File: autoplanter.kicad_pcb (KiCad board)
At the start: 2 copper layers, 99.1 x 49.5 mm, 77 parts, among them IC1 KST10MTF, IC2 KST10MTF, IC3 BME680, IC4 MCP73842T-840I_UN, J1 water, J2 USB_C_Receptacle_USB2.0, J3 Conn_01x10_Female, J4 Conn_01x02_Female, K1 Y14x-1C-xxDS, M1 Motor_DC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

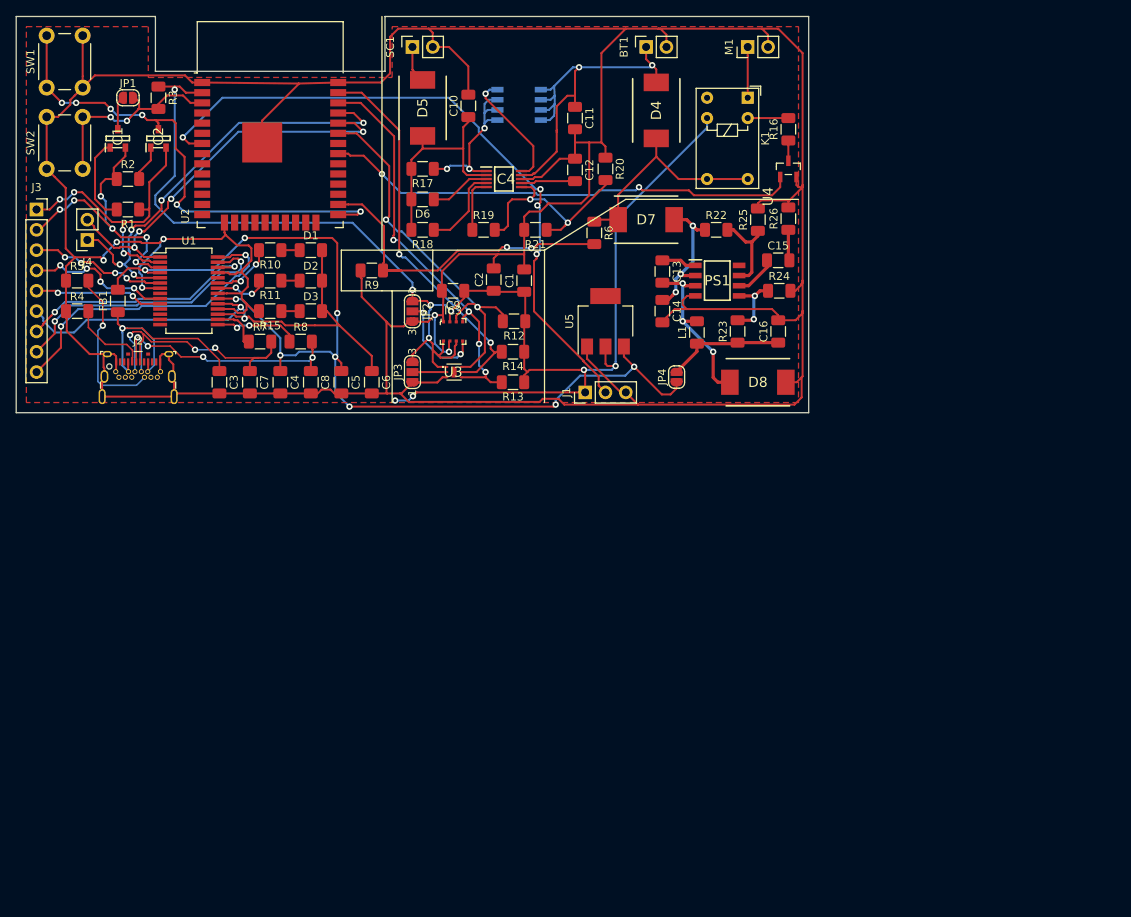
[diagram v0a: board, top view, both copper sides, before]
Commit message: Fixed regurator and added low voltage safe circuit.
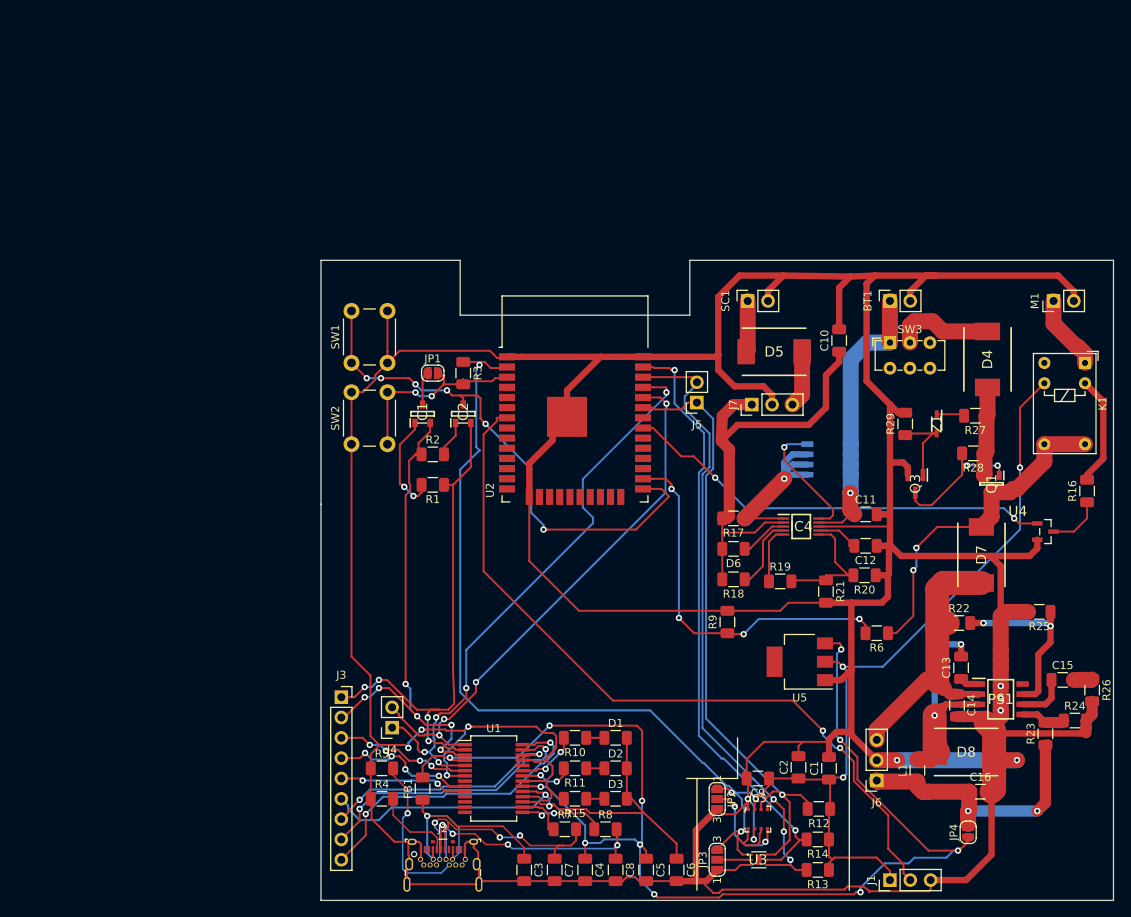
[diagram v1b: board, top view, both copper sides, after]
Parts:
- added J5: I2C Debug, Connector_PinSocket_2.54mm:PinSocket_1x02_P2.54mm_Vertical, F.Cu at (148.6, 73.7)
- added J6: external regurator, Connector_PinSocket_2.54mm:PinSocket_1x03_P2.54mm_Vertical, F.Cu at (171.1, 120.9)
- added J7: 12v regurator, Connector_PinHeader_2.54mm:PinHeader_1x03_P2.54mm_Vertical, F.Cu at (155.4, 73.9)
- added Q1: DMG2301L-7, SOT96P240X110-3N, F.Cu at (185.4, 83.8)
- added Q3: 2SC2712-Y,LF, SOT95P260X140-3N, F.Cu at (175.9, 83.8)
- added R27: 20k, Capacitor_SMD:C_1206_3216Metric, F.Cu at (183.4, 75.3)
- added R28: 20k, Capacitor_SMD:C_1206_3216Metric, F.Cu at (183.1, 80.0)
- added R29: 10k, Capacitor_SMD:C_1206_3216Metric, F.Cu at (174.6, 76.3)
- added SW3: SW_DIP_x01, Button_Switch_THT:SW_E-Switch_EG1271_DPDT, F.Cu at (172.7, 66.2)
- added Z1: MM3Z6V2T1G, SOD2512X110N, F.Cu at (178.6, 76.3)
- moved C4 71.9 mm to (134.6, 132.1)
- moved C5 71.9 mm to (142.2, 132.1)
- moved C6 71.9 mm to (146.1, 132.1)
- moved C7 71.9 mm to (130.8, 132.1)
- moved C8 71.9 mm to (138.4, 132.1)
- moved C9 71.9 mm to (156.2, 120.7)
- moved IC3 71.9 mm to (156.2, 125.7)
- moved U3 71.9 mm to (156.2, 130.8)
- moved C3 71.9 mm to (127.0, 132.1)
- moved D3 71.9 mm to (138.4, 123.2)
- moved JP3 71.9 mm to (151.1, 130.8)
- moved R13 71.9 mm to (163.7, 132.1)
- moved R14 71.9 mm to (163.7, 128.3)
- moved U1 71.9 mm to (123.2, 120.7)
- moved C2 71.9 mm to (161.3, 119.2)
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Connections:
- D4 pad 1: Net-(BT1-Pad1) -> Net-(D4-Pad1)
- D4 pad 2: +BATT -> Net-(D4-Pad2)
- D5 pad 2: Net-(C10-Pad1) -> Net-(D5-Pad2)
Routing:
- net -BATT: track 540.4 -> 680.6 mm, vias 6 -> 11
- net +5V: track 126.9 -> 157.7 mm, vias 9 -> 11
- net Net-(IC3-Pad3): track 49.2 -> 79.7 mm, vias 2 -> 1
- net Net-(IC3-Pad4): track 50.9 -> 81.3 mm, vias 4 -> 3
- net Net-(C10-Pad1): track 27.5 -> 56.5 mm
- net +3V3: track 187.3 -> 214.9 mm, vias 9 -> 7
- net Net-(R14-Pad2): track 48.6 -> 76.2 mm
- net Net-(IC1-Pad2): track 37.4 -> 63.8 mm
- net Net-(IC2-Pad2): track 37.7 -> 64.2 mm
- net Net-(C16-Pad1): track 14.8 -> 37.5 mm, vias 0 -> 2
- net Net-(J4-Pad1): track 55.3 -> 74.2 mm
- net Net-(C14-Pad1): track 17.8 -> 36.5 mm, vias 3 -> 0
- net Net-(Q1-Pad1): track 0.00 -> 18.4 mm, vias 0 -> 2
- net Net-(J4-Pad2): track 50.8 -> 68.2 mm
- net +BATT: track 27.8 -> 42.2 mm, vias 0 -> 2
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- removed copper zone on F.Cu, net -BATT
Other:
- board size 99.1 x 49.5 mm -> 99.1 x 80 mm
